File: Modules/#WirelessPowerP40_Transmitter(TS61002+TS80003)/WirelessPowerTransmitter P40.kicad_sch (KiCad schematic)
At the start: 119 parts, among them J1 USBA, J2 I2C, J3 I2C, J4 Coil Therm, J5 COIL 20uH, U1 TS30041, U2 TS94033, U3 74LVC1G66, U4 TS61002, U5 TS80003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

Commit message: wirelesspowerP40 io fix
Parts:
- J2, J3: footprint Connector_PinHeader_2.00mm:PinHeader_1x02_P2.00mm_Vertical -> Connector_PinHeader_2.00mm:PinHeader_1x04_P2.00mm_Vertical; symbol Connector:Conn_01x02_Male -> Connector:Conn_01x04_Male
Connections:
- net +3V3: now also J2.1 (Pin_1), J3.1 (Pin_1)
- net GND: now also J2.4 (Pin_4), J3.4 (Pin_4)
- net at R39.2, U5.19 (I2C|SCL): now also J2.3 (Pin_3); no longer J2.1 (Pin_1)
- net at R21.2, U5.40 (BT|TX): now also J3.3 (Pin_3); no longer J3.1 (Pin_1)

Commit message: WirelessPowerP40_Transmitter update
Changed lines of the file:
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@@
+    (stroke (width 0) (type default) (color 0 0 0 0))
+  )
+  (wire (pts (xy 195.58 231.14) (xy 213.36 231.14))
     (stroke (width 0) (type default) (color 0 0 0 0))
   )
@@
     (stroke (width 0) (type default) (color 0 0 0 0))
   )
-  (wire (pts (xy 204.47 228.6) (xy 204.47 231.14))
-    (stroke (width 0) (type default) (color 0 0 0 0))
-  )
-  (wire (pts (xy 204.47 231.14) (xy 195.58 231.14))
-    (stroke (width 0) (type default) (color 0 0 0 0))
-  )
   (wire (pts (xy 205.74 181.61) (xy 205.74 182.88))
     (stroke (width 0) (type default) (color 0 0 0 0))
@@
     (stroke (width 0) (type default) (color 0 0 0 0))
   )
-  (wire (pts (xy 210.82 228.6) (xy 204.47 228.6))
-    (stroke (width 0) (type default) (color 0 0 0 0))
-  )
-  (wire (pts (xy 210.82 228.6) (xy 210.82 231.14))
-    (stroke (width 0) (type default) (color 0 0 0 0))
-  )
-  (wire (pts (xy 210.82 231.14) (xy 213.36 231.14))
-    (stroke (width 0) (type default) (color 0 0 0 0))
-  )

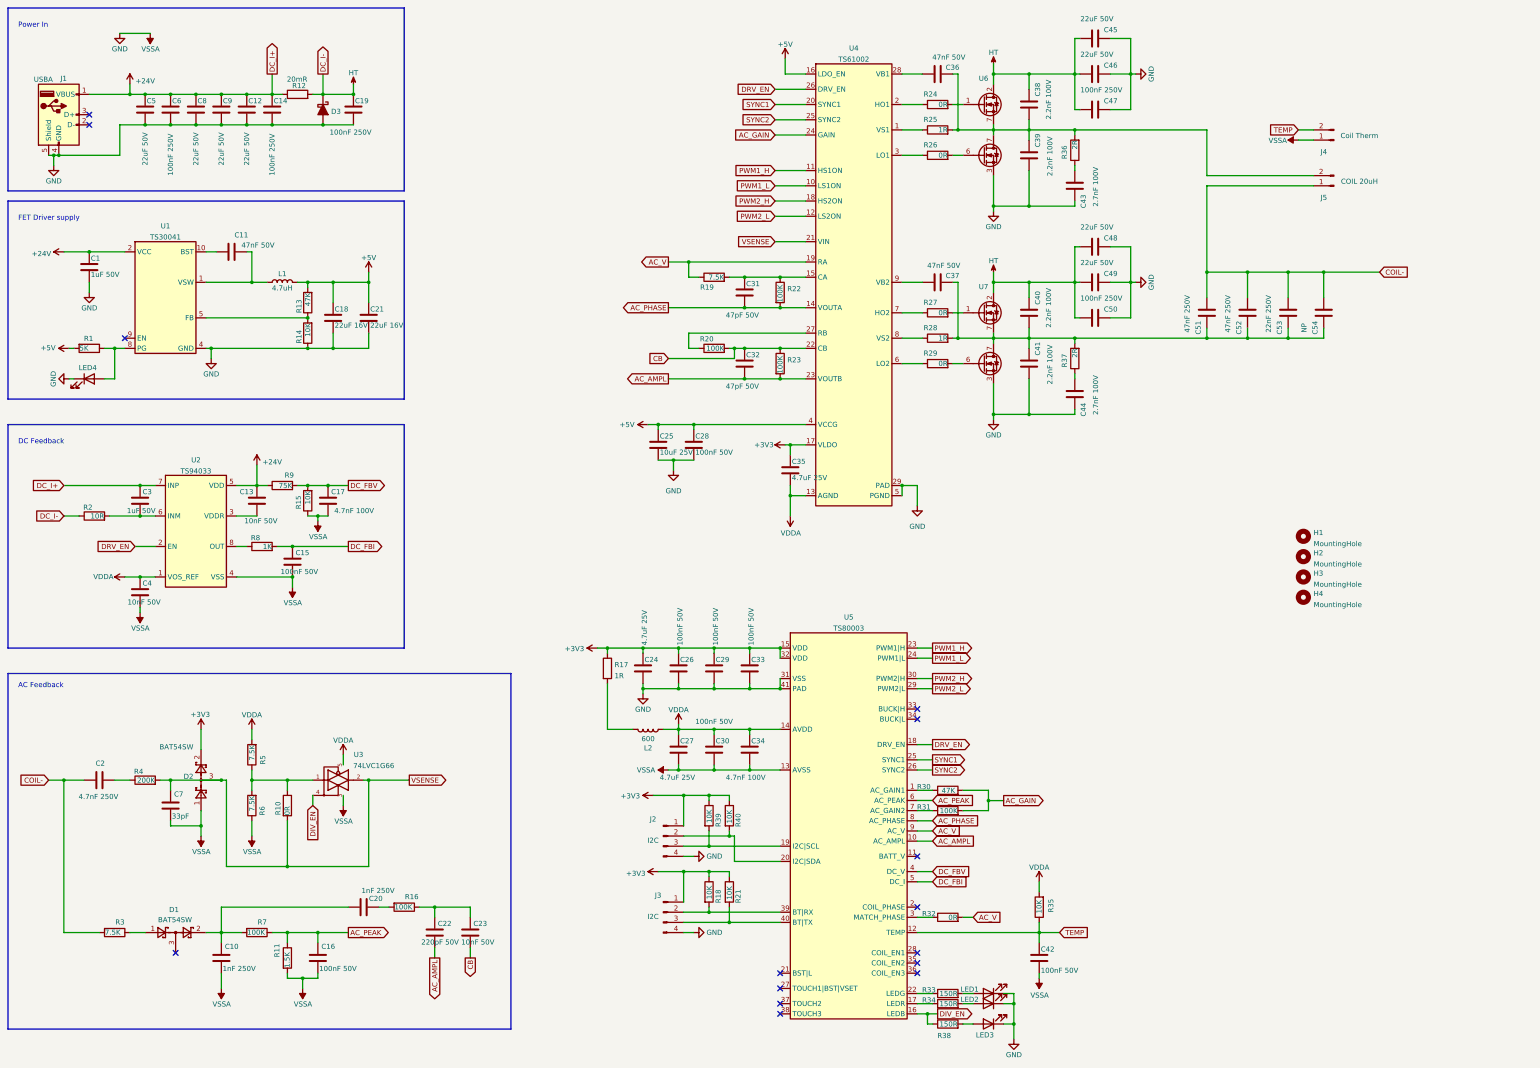
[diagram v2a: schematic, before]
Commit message: add simple cooler controller for WirelessPowerTransmitter P40
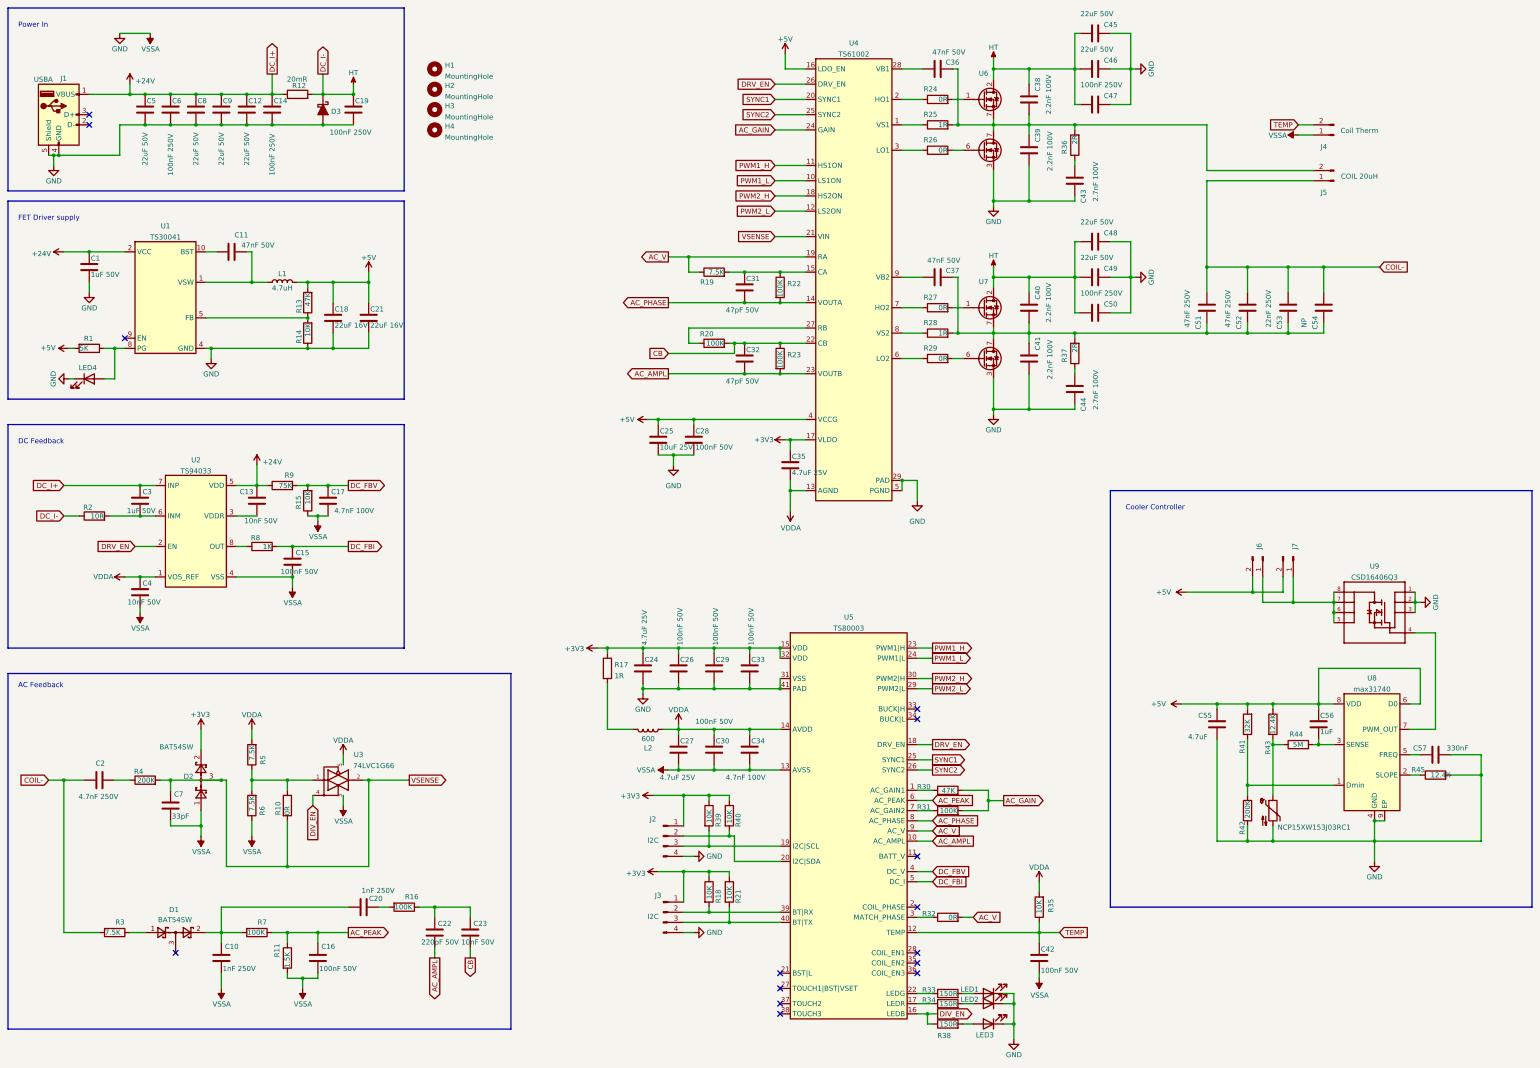
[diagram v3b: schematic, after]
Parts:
- added C55: 4.7uF, Capacitor_SMD:C_0402_1005Metric, symbol Device:C
- added C56: 1uF, Capacitor_SMD:C_0402_1005Metric, symbol Device:C
- added C57: 330nF, Capacitor_SMD:C_0402_1005Metric, symbol Device:C
- added J6, J7: Conn_01x02_Male, Connector_PinHeader_2.00mm:PinHeader_1x02_P2.00mm_Vertical, symbol Connector:Conn_01x02_Male
- added NCP15XW153J03RC1: Thermistor_NTC, Resistor_SMD:R_0402_1005Metric, symbol Device:Thermistor_NTC
- added R41: 32K, Resistor_SMD:R_0402_1005Metric, symbol Device:R
- added R42: 200K, Resistor_SMD:R_0402_1005Metric, symbol Device:R
- added R43, R45: 12.4K, Resistor_SMD:R_0402_1005Metric, symbol Device:R
- added R44: 5M, Resistor_SMD:R_0402_1005Metric, symbol Device:R
- added U8: max31740, Package_DFN_QFN:TDFN-8-1EP_3x2mm_P0.5mm_EP1.80x1.65mm, symbol MAX:max31740
- added U9: CSD16406Q3, lib:CSD16406Q3, symbol CSD16406Q3:CSD16406Q3
- C51, C52, C53, C54: footprint Inductor_SMD:L_1210_3225Metric -> Capacitor_SMD:C_1210_3225Metric
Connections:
- net +5V: now also C55.1, C56.1, J6.2 (Pin_2), J7.2 (Pin_2), R41.2, R43.1, U8.6 (D0), U8.8 (VDD)
- net GND: now also C55.2, C57.2, NCP15XW153J03RC1.2, R42.1, R45.2, U8.4 (GND), U8.9 (EP), U9.1, U9.2, U9.3
- new net: C57.1, U8.5 (FREQ)
- new net: R41.1, R42.2, U8.1 (Dmin)
- new net: U8.7 (PWM_OUT), U9.4
- new net: J6.1 (Pin_1), J7.1 (Pin_1), U9.5, U9.6, U9.7, U9.8
- new net: C56.2, R44.2, U8.3 (SENSE)
- new net: R45.1, U8.2 (SLOPE)
- new net: NCP15XW153J03RC1.1, R43.2, R44.1
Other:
- note added: "Cooler Controller"
- moved on the sheet: C25, C28, C31, C32, C35, C36, C37, C38, C39, C40, C41, C43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

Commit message: change WirelessPowerTransmitter P40 usb connector
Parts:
- J1: footprint Connector_USB:USB_A_CONNFLY_DS1095-WNR0 -> USB_plug:USB_A_2.0_FAST; symbol Connector:USB_A -> USB_Connector:USB_A_F
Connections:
- net GND: now also J1.6 (Shield); no longer J1.5 (Shield)
- no-connect marks 15 -> 16
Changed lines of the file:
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@@
   (no_connect (at 40.64 48.26))
   (no_connect (at 40.64 50.8))
+  (no_connect (at 40.64 53.34))
   (no_connect (at 49.53 104.14))
   (no_connect (at 62.23 257.81))
@@
     (pin "5")
   )
-  (symbol (lib_id "Connector:USB_A") (at 33.02 48.26 0) (unit 1)
+  (symbol (lib_id "USB_Connector:USB_A_F") (at 33.02 48.26 0) (unit 1)
     (in_bom yes) (on_board yes)
     (property "Reference" "J1" (id 0) (at 34.2265 39.2135 0))
     (property "Value" "USBA" (id 1) (at 29.1465 39.4486 0))
-    (property "Footprint" "Connector_USB:USB_A_CONNFLY_DS1095-WNR0" (id 2) (at 36.83 49.53 0)
+    (property "Footprint" "USB_plug:USB_A_2.0_FAST" (id 2) (at 36.83 49.53 0)
       (effects (font (size 1.27 1.27)) hide)
     )
@@
     (pin "4")
     (pin "5")
+    (pin "6")
   )
   (symbol (lib_id "CSD16406Q3:CSD16406Q3") (at 361.95 172.72 0) (mirror y) (unit 1)
@@
     )
     (path "/aadfb580-07ac-4146-909c-e21612e4a910"
-      (reference "J1") (unit 1) (value "USBA") (footprint "Connector_USB:USB_A_CONNFLY_DS1095-WNR0")
+      (reference "J1") (unit 1) (value "USBA") (footprint "USB_plug:USB_A_2.0_FAST")
     )
     (path "/315aa701-aff7-4924-b211-8b9bbfa38ab3"

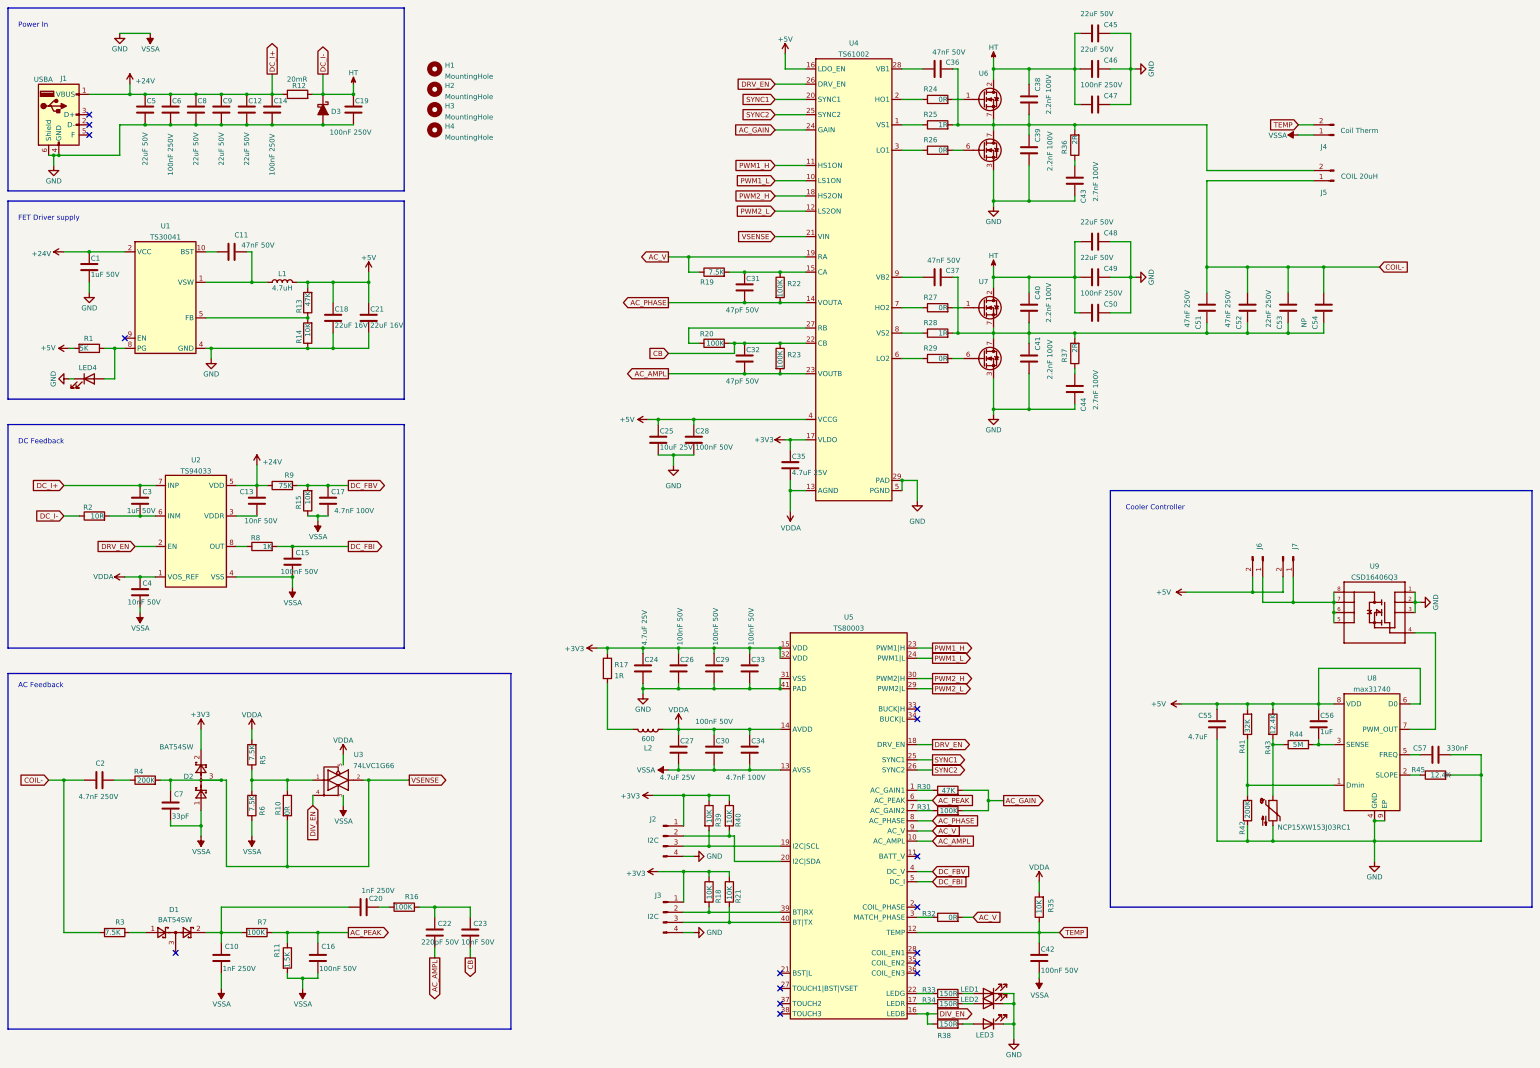
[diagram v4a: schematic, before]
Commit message: Outshape optimization of WirelessPowerTransmitterP40
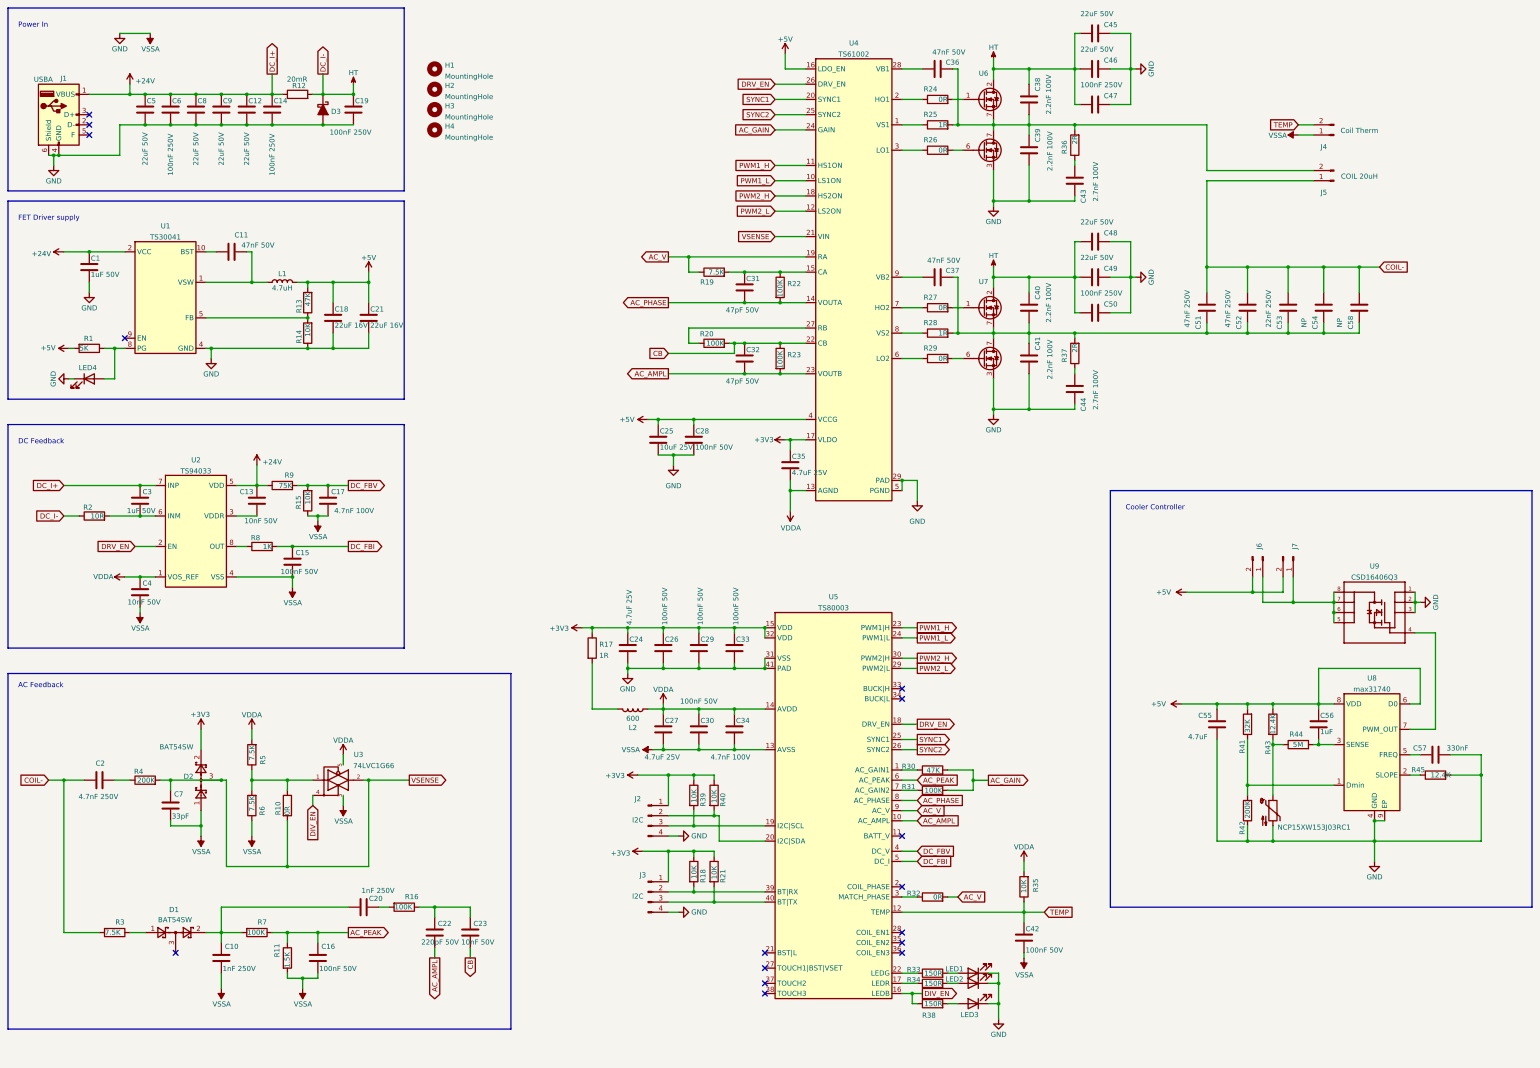
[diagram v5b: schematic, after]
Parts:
- added C58: NP, Capacitor_SMD:C_1210_3225Metric, symbol Device:C
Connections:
- net COIL-: now also C58.1
- net at C37.2, C40.1, C41.2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: now also C58.2
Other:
- moved on the sheet: C24, C26, C27, C29, C30, C33, C34, C42, J2, J3, L2, LED1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

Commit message: update bom
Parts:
- R1: value 5K -> 5.1K
- R41: value 32K -> 33K
- R44: value 5M -> 5.1M
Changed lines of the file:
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@@
       (effects (font (size 1.27 1.27)) (justify left))
     )
-    (property "Value" "5K" (id 1) (at 38.1875 106.6419 90)
+    (property "Value" "5.1K" (id 1) (at 38.1875 106.6419 90)
       (effects (font (size 1.27 1.27)) (justify left))
     )
@@
       (effects (font (size 1.27 1.27)) (justify left))
     )
-    (property "Value" "32K" (id 1) (at 330.2037 199.42 90)
+    (property "Value" "33K" (id 1) (at 330.2037 199.42 90)
       (effects (font (size 1.27 1.27)) (justify left))
     )
@@
   (symbol (lib_id "Device:R") (at 342.9 205.74 90) (unit 1)
     (in_bom yes) (on_board yes)
-    (property "Reference" "R44" (id 0) (at 344.1001 203.1572 90)
-      (effects (font (size 1.27 1.27)) (justify left))
-    )
-    (property "Value" "5M" (id 1) (at 344.14 205.7437 90)
+    (property "Reference" "R44" (id 0) (at 344.1001 205.6972 90)
+      (effects (font (size 1.27 1.27)) (justify left))
+    )
+    (property "Value" "5.1M" (id 1) (at 345.41 208.2837 90)
       (effects (font (size 1.27 1.27)) (justify left))
     )
@@
     )
     (path "/439b9c70-b82d-4006-83a2-9e7b401b9615"
-      (reference "R1") (unit 1) (value "5K") (footprint "Resistor_SMD:R_0402_1005Metric")
+      (reference "R1") (unit 1) (value "5.1K") (footprint "Resistor_SMD:R_0402_1005Metric")
     )
     (path "/f3733936-b166-47df-bf52-a8b4dfc98a97"
@@
     )
     (path "/479a34f3-f0e2-4c4c-878f-9bad504ba942"
-      (reference "R41") (unit 1) (value "32K") (footprint "Resistor_SMD:R_0402_1005Metric")
+      (reference "R41") (unit 1) (value "33K") (footprint "Resistor_SMD:R_0402_1005Metric")
     )
     (path "/55d2995f-03b7-419c-9da8-70fa8363cdd4"
@@
     )
     (path "/f1c9c72c-98e0-4cd0-ae21-2eb278856b56"
-      (reference "R44") (unit 1) (value "5M") (footprint "Resistor_SMD:R_0402_1005Metric")
+      (reference "R44") (unit 1) (value "5.1M") (footprint "Resistor_SMD:R_0402_1005Metric")
     )
     (path "/a97ffacd-f0eb-4c90-bfef-a146eda91bf6"
